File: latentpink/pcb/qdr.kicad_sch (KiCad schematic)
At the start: 69 parts, among them U2 XC7K160T-2FBG484C, U28 IS25WP256D-JLLE, U29 DSC1123CI2-150.0000T, U3 CY7C2245KV18-450BZXI

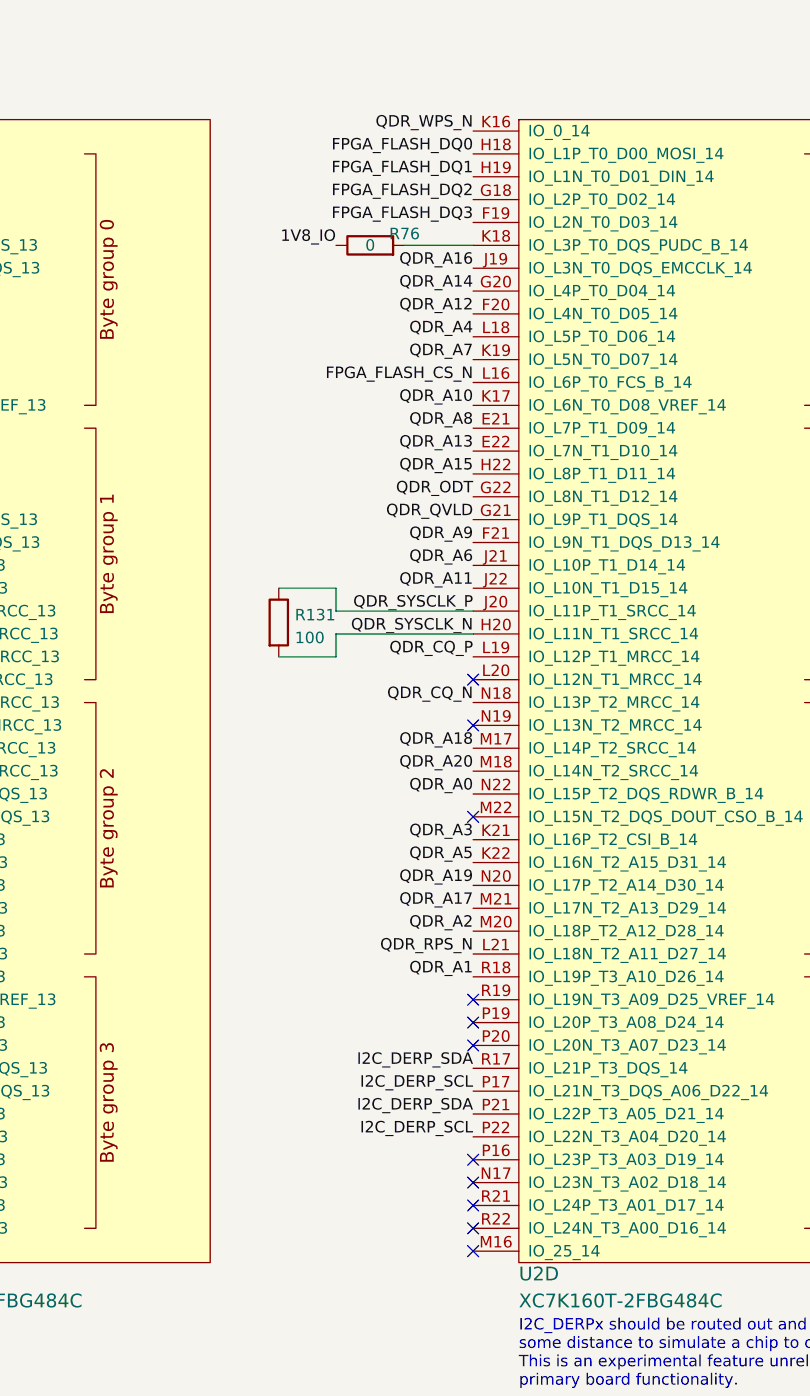
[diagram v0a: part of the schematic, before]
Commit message: Moved QDR to wide orientation, preliminary layout (no length matching) of C/A bus
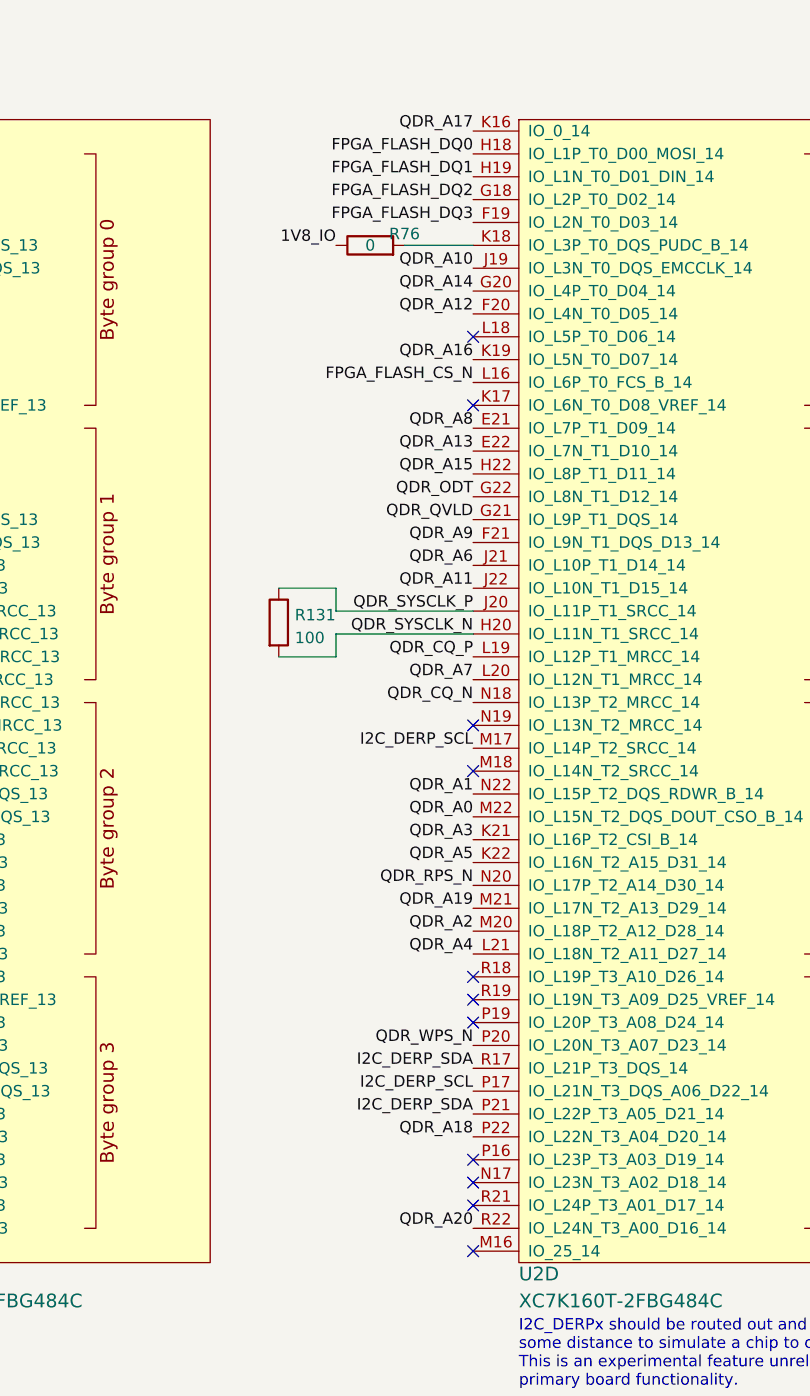
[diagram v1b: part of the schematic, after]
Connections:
- net I2C_DERP_SCL: now also U2.M17 (IO_L14P_T2_SRCC_14); no longer U2.P22 (IO_L22N_T3_A04_D20_14)
- net QDR_A0: now also U2.M22 (IO_L15N_T2_DQS_DOUT_CSO_B_14); no longer U2.N22 (IO_L15P_T2_DQS_RDWR_B_14)
- net QDR_A1: now also U2.N22 (IO_L15P_T2_DQS_RDWR_B_14); no longer U2.R18 (IO_L19P_T3_A10_D26_14)
- net QDR_A10: now also U2.J19 (IO_L3N_T0_DQS_EMCCLK_14); no longer U2.K17 (IO_L6N_T0_D08_VREF_14)
- net QDR_A16: now also U2.K19 (IO_L5N_T0_D07_14); no longer U2.J19 (IO_L3N_T0_DQS_EMCCLK_14)
- net QDR_A17: now also U2.K16 (IO_0_14); no longer U2.M21 (IO_L17N_T2_A13_D29_14)
- net QDR_A18: now also U2.P22 (IO_L22N_T3_A04_D20_14); no longer U2.M17 (IO_L14P_T2_SRCC_14)
- net QDR_A19: now also U2.M21 (IO_L17N_T2_A13_D29_14); no longer U2.N20 (IO_L17P_T2_A14_D30_14)
- net QDR_A20: now also U2.R22 (IO_L24N_T3_A00_D16_14); no longer U2.M18 (IO_L14N_T2_SRCC_14)
- net QDR_A4: now also U2.L21 (IO_L18N_T2_A11_D27_14); no longer U2.L18 (IO_L5P_T0_D06_14)
- net QDR_A7: now also U2.L20 (IO_L12N_T1_MRCC_14); no longer U2.K19 (IO_L5N_T0_D07_14)
- net QDR_RPS_N: now also U2.N20 (IO_L17P_T2_A14_D30_14); no longer U2.L21 (IO_L18N_T2_A11_D27_14)
- net QDR_WPS_N: now also U2.P20 (IO_L20N_T3_A07_D23_14); no longer U2.K16 (IO_0_14)
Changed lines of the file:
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@@
   (junction (at 210.82 243.84) (diameter 0) (color 0 0 0 0)
   )
-  (no_connect (at 269.24 127))
   (no_connect (at 346.71 68.58))
   (no_connect (at 269.24 142.24))
@@
   (no_connect (at 346.71 38.1))
   (no_connect (at 269.24 149.86))
+  (no_connect (at 269.24 48.26))
   (no_connect (at 198.12 132.08))
   (no_connect (at 346.71 101.6))
-  (no_connect (at 269.24 101.6))
+  (no_connect (at 269.24 55.88))
+  (no_connect (at 269.24 96.52))
   (no_connect (at 269.24 121.92))
   (no_connect (at 198.12 40.64))
@@
   (no_connect (at 346.71 149.86))
   (no_connect (at 200.66 264.16))
-  (no_connect (at 269.24 147.32))
   (no_connect (at 33.02 179.07))
   (no_connect (at 269.24 91.44))
@@
   (no_connect (at 198.12 149.86))
   (no_connect (at 346.71 86.36))
-  (no_connect (at 269.24 86.36))
+  (no_connect (at 269.24 119.38))
   (wire (pts (xy 88.9 209.55) (xy 101.6 209.55))
     (stroke (width 0) (type default) (color 0 0 0 0))
@@
     (effects (font (size 1.27 1.27)) (justify right bottom))
   )
-  (label "QDR_A18" (at 269.24 93.98 180)
+  (label "QDR_A18" (at 269.24 137.16 180)
     (effects (font (size 1.27 1.27)) (justify right bottom))
   )
@@
     (effects (font (size 1.27 1.27)) (justify right bottom))
   )
-  (label "QDR_A0" (at 269.24 99.06 180)
+  (label "QDR_A0" (at 269.24 101.6 180)
     (effects (font (size 1.27 1.27)) (justify right bottom))
   )
@@
     (effects (font (size 1.27 1.27)) (justify right bottom))
   )
-  (label "QDR_A20" (at 269.24 96.52 180)
+  (label "QDR_A20" (at 269.24 147.32 180)
     (effects (font (size 1.27 1.27)) (justify right bottom))
   )
@@
     (effects (font (size 1.27 1.27)) (justify right bottom))
   )
-  (label "QDR_A1" (at 269.24 119.38 180)
+  (label "QDR_A1" (at 269.24 99.06 180)
     (effects (font (size 1.27 1.27)) (justify right bottom))
   )
@@
     (effects (font (size 1.27 1.27)) (justify right bottom))
   )
-  (label "QDR_WPS_N" (at 269.24 25.4 180)
+  (label "QDR_WPS_N" (at 269.24 127 180)
     (effects (font (size 1.27 1.27)) (justify right bottom))
   )
@@
     (effects (font (size 1.27 1.27)) (justify right bottom))
   )
-  (label "QDR_A19" (at 269.24 109.22 180)
+  (label "QDR_A19" (at 269.24 111.76 180)
     (effects (font (size 1.27 1.27)) (justify right bottom))
   )
@@
     (effects (font (size 1.27 1.27)) (justify right bottom))
   )
-  (label "QDR_A17" (at 269.24 111.76 180)
+  (label "QDR_A17" (at 269.24 25.4 180)
     (effects (font (size 1.27 1.27)) (justify right bottom))
   )
@@
     (effects (font (size 1.27 1.27)) (justify right bottom))
   )
-  (label "QDR_RPS_N" (at 269.24 116.84 180)
+  (label "QDR_RPS_N" (at 269.24 109.22 180)
     (effects (font (size 1.27 1.27)) (justify right bottom))
   )
@@
     (effects (font (size 1.27 1.27)) (justify right bottom))
   )
-  (label "QDR_A4" (at 269.24 48.26 180)
+  (label "QDR_A4" (at 269.24 116.84 180)
     (effects (font (size 1.27 1.27)) (justify right bottom))
   )
@@
     (effects (font (size 1.27 1.27)) (justify right bottom))
   )
-  (label "QDR_A10" (at 269.24 55.88 180)
+  (label "QDR_A10" (at 269.24 40.64 180)
     (effects (font (size 1.27 1.27)) (justify right bottom))
   )
@@
     (effects (font (size 1.27 1.27)) (justify right bottom))
   )
-  (label "QDR_A16" (at 269.24 40.64 180)
+  (label "QDR_A16" (at 269.24 50.8 180)
     (effects (font (size 1.27 1.27)) (justify right bottom))
   )
@@
     (effects (font (size 1.27 1.27)) (justify right bottom))
   )
-  (label "QDR_A7" (at 269.24 50.8 180)
+  (label "QDR_A7" (at 269.24 86.36 180)
     (effects (font (size 1.27 1.27)) (justify right bottom))
   )
@@
     (effects (font (size 1.27 1.27)) (justify right bottom))
   )
-  (label "I2C_DERP_SCL" (at 269.24 137.16 180)
-    (effects (font (size 1.27 1.27)) (justify right bottom))
-  )
+  (label "I2C_DERP_SCL" (at 269.24 93.98 180)
+    (effects (font (size 1.27 1.27)) (justify right bottom))
+  )

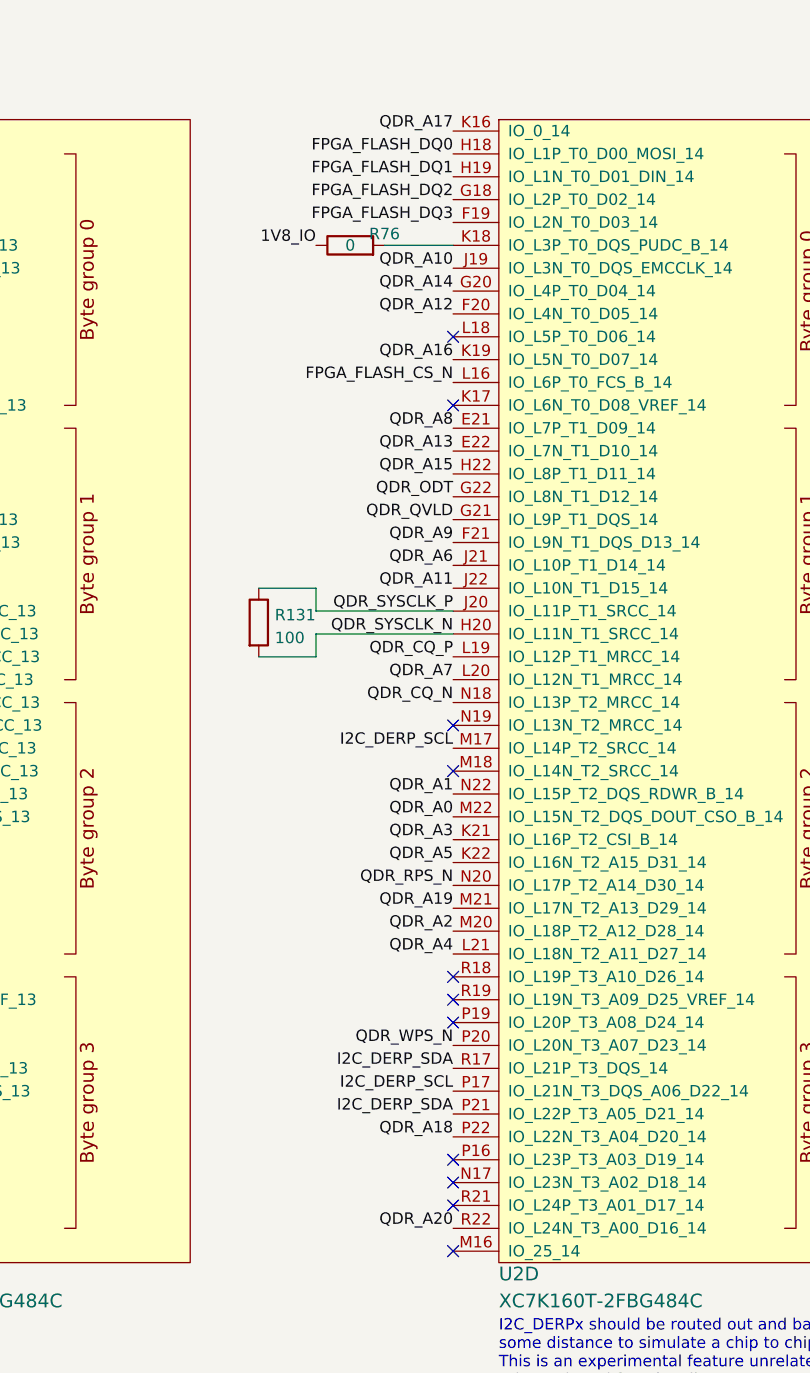
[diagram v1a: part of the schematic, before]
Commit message: Lots of cleanup of C/A bus
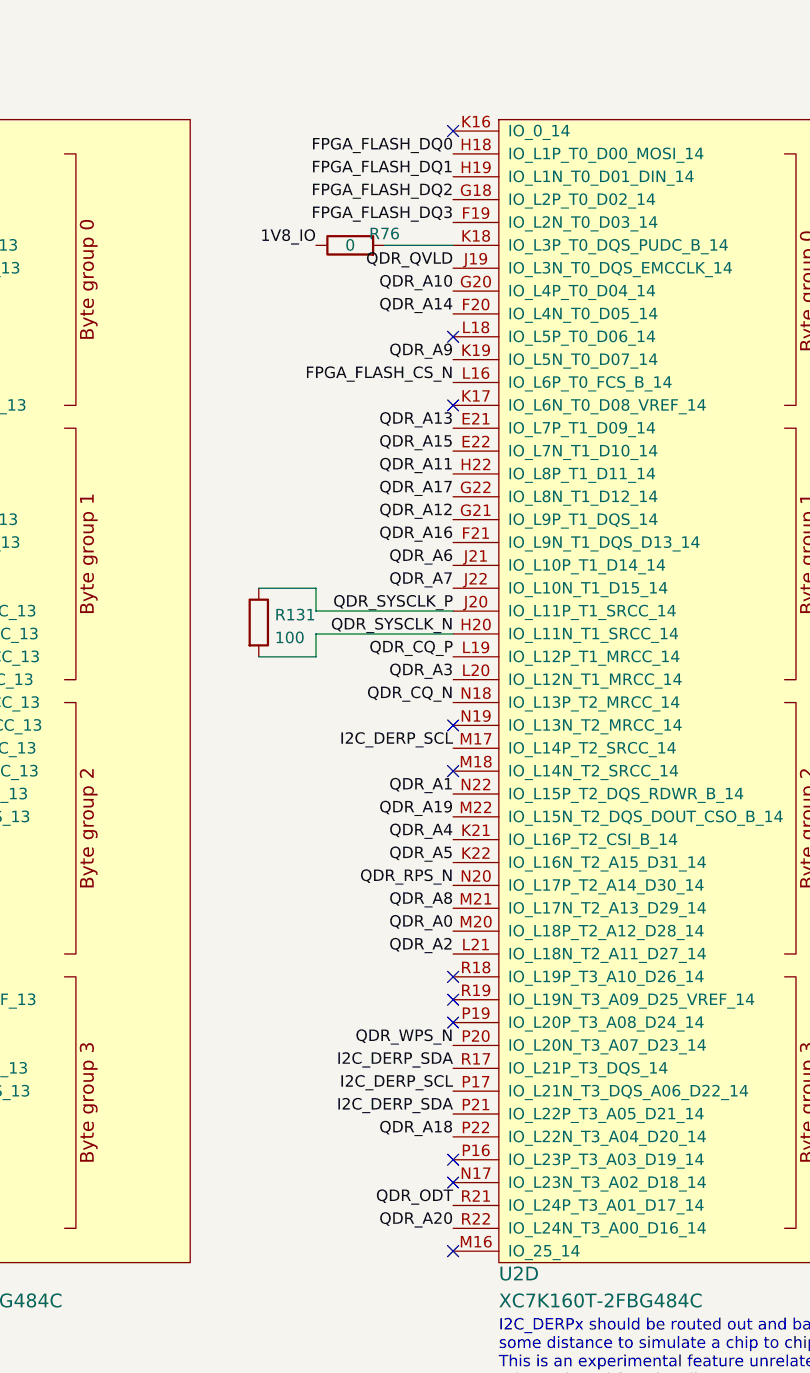
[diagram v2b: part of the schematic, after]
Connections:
- net QDR_A0: now also U2.M20 (IO_L18P_T2_A12_D28_14); no longer U2.M22 (IO_L15N_T2_DQS_DOUT_CSO_B_14)
- net QDR_A10: now also U2.G20 (IO_L4P_T0_D04_14); no longer U2.J19 (IO_L3N_T0_DQS_EMCCLK_14)
- net QDR_A11: now also U2.H22 (IO_L8P_T1_D11_14); no longer U2.J22 (IO_L10N_T1_D15_14)
- net QDR_A12: now also U2.G21 (IO_L9P_T1_DQS_14); no longer U2.F20 (IO_L4N_T0_D05_14)
- net QDR_A13: now also U2.E21 (IO_L7P_T1_D09_14); no longer U2.E22 (IO_L7N_T1_D10_14)
- net QDR_A14: now also U2.F20 (IO_L4N_T0_D05_14); no longer U2.G20 (IO_L4P_T0_D04_14)
- net QDR_A15: now also U2.E22 (IO_L7N_T1_D10_14); no longer U2.H22 (IO_L8P_T1_D11_14)
- net QDR_A16: now also U2.F21 (IO_L9N_T1_DQS_D13_14); no longer U2.K19 (IO_L5N_T0_D07_14)
- net QDR_A17: now also U2.G22 (IO_L8N_T1_D12_14); no longer U2.K16 (IO_0_14)
- net QDR_A19: now also U2.M22 (IO_L15N_T2_DQS_DOUT_CSO_B_14); no longer U2.M21 (IO_L17N_T2_A13_D29_14)
- net QDR_A2: now also U2.L21 (IO_L18N_T2_A11_D27_14); no longer U2.M20 (IO_L18P_T2_A12_D28_14)
- net QDR_A3: now also U2.L20 (IO_L12N_T1_MRCC_14); no longer U2.K21 (IO_L16P_T2_CSI_B_14)
- net QDR_A4: now also U2.K21 (IO_L16P_T2_CSI_B_14); no longer U2.L21 (IO_L18N_T2_A11_D27_14)
- net QDR_A7: now also U2.J22 (IO_L10N_T1_D15_14); no longer U2.L20 (IO_L12N_T1_MRCC_14)
- net QDR_A8: now also U2.M21 (IO_L17N_T2_A13_D29_14); no longer U2.E21 (IO_L7P_T1_D09_14)
- net QDR_A9: now also U2.K19 (IO_L5N_T0_D07_14); no longer U2.F21 (IO_L9N_T1_DQS_D13_14)
- net QDR_ODT: now also U2.R21 (IO_L24P_T3_A01_D17_14); no longer U2.G22 (IO_L8N_T1_D12_14)
- net QDR_QVLD: now also U2.J19 (IO_L3N_T0_DQS_EMCCLK_14); no longer U2.G21 (IO_L9P_T1_DQS_14)
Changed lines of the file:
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@@
   (no_connect (at 346.71 68.58))
   (no_connect (at 269.24 142.24))
-  (no_connect (at 269.24 144.78))
   (no_connect (at 198.12 25.4))
   (no_connect (at 346.71 132.08))
@@
   (no_connect (at 346.71 101.6))
   (no_connect (at 269.24 55.88))
+  (no_connect (at 269.24 25.4))
   (no_connect (at 269.24 96.52))
   (no_connect (at 269.24 121.92))
@@
     (effects (font (size 1.27 1.27)) (justify right bottom))
   )
-  (label "QDR_A3" (at 269.24 104.14 180)
+  (label "QDR_A3" (at 269.24 86.36 180)
     (effects (font (size 1.27 1.27)) (justify right bottom))
   )
@@
     (effects (font (size 1.27 1.27)) (justify right bottom))
   )
-  (label "QDR_A0" (at 269.24 101.6 180)
+  (label "QDR_A0" (at 269.24 114.3 180)
     (effects (font (size 1.27 1.27)) (justify right bottom))
   )
@@
     (effects (font (size 1.27 1.27)) (justify right bottom))
   )
-  (label "QDR_A9" (at 269.24 71.12 180)
+  (label "QDR_A9" (at 269.24 50.8 180)
     (effects (font (size 1.27 1.27)) (justify right bottom))
   )
@@
     (effects (font (size 1.27 1.27)) (justify right bottom))
   )
-  (label "QDR_A11" (at 269.24 76.2 180)
+  (label "QDR_A11" (at 269.24 63.5 180)
     (effects (font (size 1.27 1.27)) (justify right bottom))
   )
@@
     (effects (font (size 1.27 1.27)) (justify right bottom))
   )
-  (label "QDR_A15" (at 269.24 63.5 180)
-    (effects (font (size 1.27 1.27)) (justify right bottom))
-  )
-  (label "QDR_A8" (at 269.24 58.42 180)
+  (label "QDR_A15" (at 269.24 60.96 180)
+    (effects (font (size 1.27 1.27)) (justify right bottom))
+  )
+  (label "QDR_A8" (at 269.24 111.76 180)
     (effects (font (size 1.27 1.27)) (justify right bottom))
   )
@@
     (effects (font (size 1.27 1.27)) (justify right bottom))
   )
-  (label "QDR_A14" (at 269.24 43.18 180)
+  (label "QDR_A14" (at 269.24 45.72 180)
     (effects (font (size 1.27 1.27)) (justify right bottom))
   )
@@
     (effects (font (size 1.27 1.27)) (justify right bottom))
   )
-  (label "QDR_A12" (at 269.24 45.72 180)
+  (label "QDR_A12" (at 269.24 68.58 180)
     (effects (font (size 1.27 1.27)) (justify right bottom))
   )
@@
     (effects (font (size 1.27 1.27)) (justify right bottom))
   )
-  (label "QDR_A19" (at 269.24 111.76 180)
+  (label "QDR_A19" (at 269.24 101.6 180)
     (effects (font (size 1.27 1.27)) (justify right bottom))
   )
@@
     (effects (font (size 1.27 1.27)) (justify right bottom))
   )
-  (label "QDR_A17" (at 269.24 25.4 180)
+  (label "QDR_A17" (at 269.24 66.04 180)
     (effects (font (size 1.27 1.27)) (justify right bottom))
   )
@@
     (effects (font (size 1.27 1.27)) (justify right bottom))
   )
-  (label "QDR_A4" (at 269.24 116.84 180)
+  (label "QDR_A4" (at 269.24 104.14 180)
     (effects (font (size 1.27 1.27)) (justify right bottom))
   )
@@
     (effects (font (size 1.27 1.27)) (justify right bottom))
   )
-  (label "QDR_A2" (at 269.24 114.3 180)
+  (label "QDR_A2" (at 269.24 116.84 180)
     (effects (font (size 1.27 1.27)) (justify right bottom))
   )
@@
     (effects (font (size 1.27 1.27)) (justify right bottom))
   )
-  (label "QDR_ODT" (at 269.24 66.04 180)
+  (label "QDR_ODT" (at 269.24 144.78 180)
     (effects (font (size 1.27 1.27)) (justify right bottom))
   )
@@
     (effects (font (size 1.27 1.27)) (justify right bottom))
   )
-  (label "QDR_QVLD" (at 269.24 68.58 180)
+  (label "QDR_QVLD" (at 269.24 40.64 180)
     (effects (font (size 1.27 1.27)) (justify right bottom))
   )
@@
     (effects (font (size 1.27 1.27)) (justify right bottom))
   )
-  (label "QDR_A13" (at 269.24 60.96 180)
+  (label "QDR_A13" (at 269.24 58.42 180)
     (effects (font (size 1.27 1.27)) (justify right bottom))
   )
@@
     (effects (font (size 1.27 1.27)) (justify right bottom))
   )
-  (label "QDR_A10" (at 269.24 40.64 180)
+  (label "QDR_A10" (at 269.24 43.18 180)
     (effects (font (size 1.27 1.27)) (justify right bottom))
   )
@@
     (effects (font (size 1.27 1.27)) (justify right bottom))
   )
-  (label "QDR_A16" (at 269.24 50.8 180)
+  (label "QDR_A16" (at 269.24 71.12 180)
     (effects (font (size 1.27 1.27)) (justify right bottom))
   )
@@
     (effects (font (size 1.27 1.27)) (justify right bottom))
   )
-  (label "QDR_A7" (at 269.24 86.36 180)
-    (effects (font (size 1.27 1.27)) (justify right bottom))
-  )
+  (label "QDR_A7" (at 269.24 76.2 180)
+    (effects (font (size 1.27 1.27)) (justify right bottom))
+  )
